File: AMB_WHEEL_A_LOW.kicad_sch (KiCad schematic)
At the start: 14 parts, among them U13 EPC2152, U14 EPC2152

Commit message: updated layouts, added motor
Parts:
- renumbered C103 to C127, C104 to C128, C105 to C129, C106 to C130, C107 to C131, C108 to C132, C109 to C133, C110 to C134, R75 to R131, R76 to R132, R77 to R133, R78 to R134, U13 to U11, U14 to U12

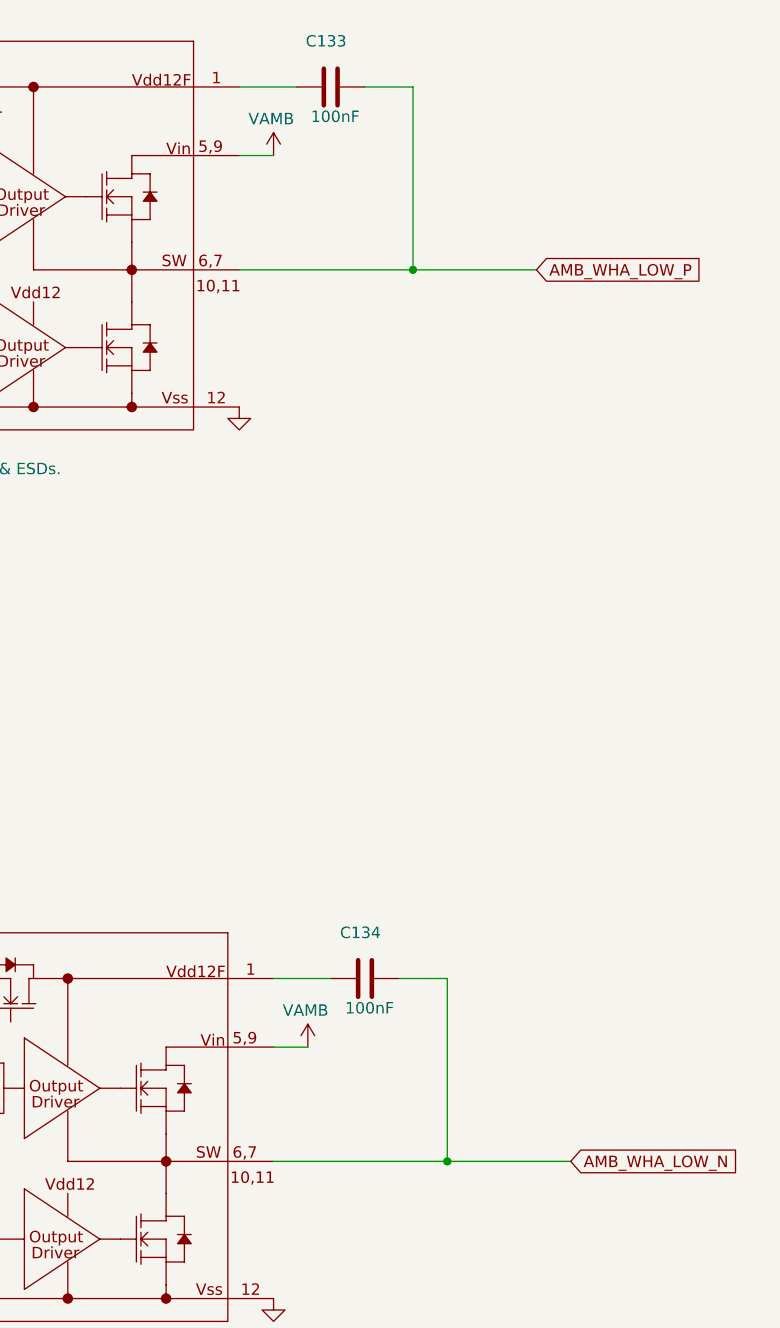
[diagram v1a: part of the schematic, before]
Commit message: Changes to layout pins
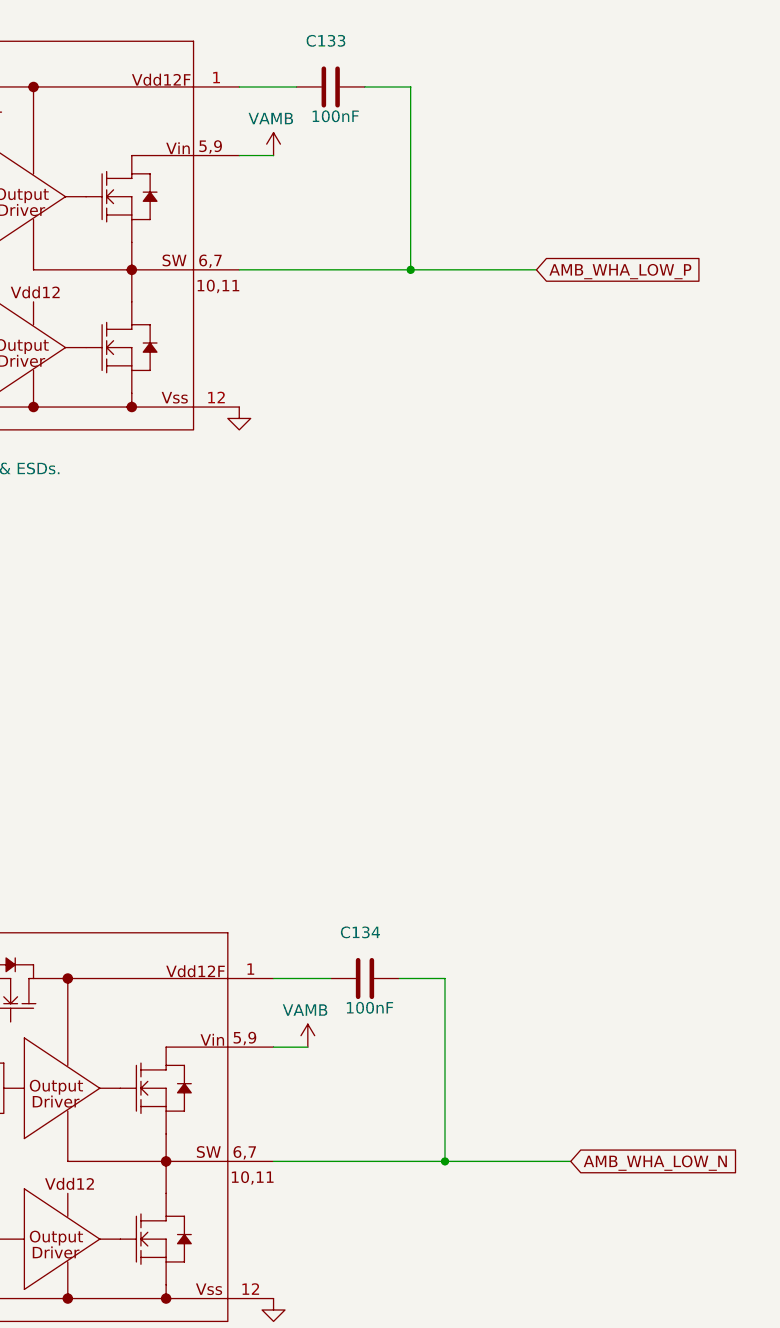
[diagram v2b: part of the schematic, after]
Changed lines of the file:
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@@
 	)
 	(junction
-		(at 189.484 58.42)
+		(at 189.23 58.42)
 		(diameter 0)
 		(color 0 0 0 0)
@@
 	)
 	(junction
-		(at 193.294 157.48)
+		(at 193.04 157.48)
 		(diameter 0)
 		(color 0 0 0 0)
@@
 	(wire
 		(pts
-			(xy 189.484 58.42) (xy 203.2 58.42)
+			(xy 189.23 58.42) (xy 203.2 58.42)
 		)
 		(stroke
@@
 	(wire
 		(pts
-			(xy 187.96 137.16) (xy 193.294 137.16)
+			(xy 187.96 137.16) (xy 193.04 137.16)
 		)
 		(stroke
@@
 	(wire
 		(pts
-			(xy 189.484 38.1) (xy 189.484 58.42)
+			(xy 189.23 38.1) (xy 189.23 58.42)
 		)
 		(stroke
@@
 	(wire
 		(pts
-			(xy 173.99 157.48) (xy 193.294 157.48)
+			(xy 173.99 157.48) (xy 193.04 157.48)
 		)
 		(stroke
@@
 	(wire
 		(pts
-			(xy 193.294 157.48) (xy 207.01 157.48)
+			(xy 193.04 157.48) (xy 207.01 157.48)
 		)
 		(stroke
@@
 	(wire
 		(pts
-			(xy 184.15 38.1) (xy 189.484 38.1)
+			(xy 184.15 38.1) (xy 189.23 38.1)
 		)
 		(stroke
@@
 	(wire
 		(pts
-			(xy 193.294 137.16) (xy 193.294 157.48)
+			(xy 193.04 137.16) (xy 193.04 157.48)
 		)
 		(stroke
@@
 	(wire
 		(pts
-			(xy 170.18 58.42) (xy 189.484 58.42)
+			(xy 170.18 58.42) (xy 189.23 58.42)
 		)
 		(stroke
@@
 	)
 	(symbol
-		(lib_id "CIAA_ACC:GND")
+		(lib_id "power:GND")
 		(at 170.18 73.66 0)
 		(unit 1)
@@
 		(property "Footprint" ""
 			(at 170.18 73.66 0)
+			(hide yes)
 			(show_name no)
 			(do_not_autoplace no)
@@
 		(property "Datasheet" ""
 			(at 170.18 73.66 0)
+			(hide yes)
 			(show_name no)
 			(do_not_autoplace no)
@@
 			)
 		)
-		(property "Description" ""
+		(property "Description" "Power symbol creates a global label with name \"GND\" , ground"
 			(at 170.18 73.66 0)
+			(hide yes)
 			(show_name no)
 			(do_not_autoplace no)
@@
 	)
 	(symbol
-		(lib_id "CIAA_ACC:GND")
+		(lib_id "power:GND")
 		(at 173.99 172.72 0)
 		(unit 1)
@@
 		(property "Footprint" ""
 			(at 173.99 172.72 0)
+			(hide yes)
 			(show_name no)
 			(do_not_autoplace no)
@@
 		(property "Datasheet" ""
 			(at 173.99 172.72 0)
+			(hide yes)
 			(show_name no)
 			(do_not_autoplace no)
@@
 			)
 		)
-		(property "Description" ""
+		(property "Description" "Power symbol creates a global label with name \"GND\" , ground"
 			(at 173.99 172.72 0)
+			(hide yes)
 			(show_name no)
 			(do_not_autoplace no)
@@
 	)
 	(symbol
-		(lib_id "CIAA_ACC:GND")
+		(lib_id "power:GND")
 		(at 109.22 73.66 0)
 		(unit 1)
@@
 		(property "Footprint" ""
 			(at 109.22 73.66 0)
+			(hide yes)
 			(show_name no)
 			(do_not_autoplace no)
@@
 		(property "Datasheet" ""
 			(at 109.22 73.66 0)
+			(hide yes)
 			(show_name no)
 			(do_not_autoplace no)
@@
 			)
 		)
-		(property "Description" ""
+		(property "Description" "Power symbol creates a global label with name \"GND\" , ground"
 			(at 109.22 73.66 0)
+			(hide yes)
 			(show_name no)
 			(do_not_autoplace no)
@@
 	)
 	(symbol
-		(lib_id "CIAA_ACC:GND")
+		(lib_id "power:GND")
 		(at 77.47 72.39 0)
 		(unit 1)
@@
 		(property "Footprint" ""
 			(at 77.47 72.39 0)
+			(hide yes)
 			(show_name no)
 			(do_not_autoplace no)
@@
 		(property "Datasheet" ""
 			(at 77.47 72.39 0)
+			(hide yes)
 			(show_name no)
 			(do_not_autoplace no)
@@
 			)
 		)
-		(property "Description" ""
+		(property "Description" "Power symbol creates a global label with name \"GND\" , ground"
 			(at 77.47 72.39 0)
+			(hide yes)
 			(show_name no)
 			(do_not_autoplace no)
@@
 	)
 	(symbol
-		(lib_id "CIAA_ACC:GND")
+		(lib_id "power:GND")
 		(at 104.14 46.99 0)
 		(unit 1)
@@
 		(property "Footprint" ""
 			(at 104.14 46.99 0)
+			(hide yes)
 			(show_name no)
 			(do_not_autoplace no)
@@
 		(property "Datasheet" ""
 			(at 104.14 46.99 0)
+			(hide yes)
 			(show_name no)
 			(do_not_autoplace no)
@@
 			)
 		)
-		(property "Description" ""
+		(property "Description" "Power symbol creates a global label with name \"GND\" , ground"
 			(at 104.14 46.99 0)
+			(hide yes)
 			(show_name no)
 			(do_not_autoplace no)
@@
 	)
 	(symbol
-		(lib_id "CIAA_ACC:GND")
+		(lib_id "power:GND")
 		(at 81.28 171.45 0)
 		(unit 1)
@@
 		(property "Footprint" ""
 			(at 81.28 171.45 0)
+			(hide yes)
 			(show_name no)
 			(do_not_autoplace no)
@@
 		(property "Datasheet" ""
 			(at 81.28 171.45 0)
+			(hide yes)
 			(show_name no)
 			(do_not_autoplace no)
@@
 			)
 		)
-		(property "Description" ""
+		(property "Description" "Power symbol creates a global label with name \"GND\" , ground"
 			(at 81.28 171.45 0)
+			(hide yes)
 			(show_name no)
 			(do_not_autoplace no)
@@
 	)
 	(symbol
-		(lib_id "CIAA_ACC:GND")
+		(lib_id "power:GND")
 		(at 85.09 156.21 0)
 		(unit 1)
@@
 		(property "Footprint" ""
 			(at 85.09 156.21 0)
+			(hide yes)
 			(show_name no)
 			(do_not_autoplace no)
@@
 		(property "Datasheet" ""
 			(at 85.09 156.21 0)
+			(hide yes)
 			(show_name no)
 			(do_not_autoplace no)
@@
 			)
 		)
-		(property "Description" ""
+		(property "Description" "Power symbol creates a global label with name \"GND\" , ground"
 			(at 85.09 156.21 0)
+			(hide yes)
 			(show_name no)
 			(do_not_autoplace no)
@@
 	)
 	(symbol
-		(lib_id "CIAA_ACC:GND")
+		(lib_id "power:GND")
 		(at 107.95 146.05 0)
 		(unit 1)
@@
 		(property "Footprint" ""
 			(at 107.95 146.05 0)
+			(hide yes)
 			(show_name no)
 			(do_not_autoplace no)
@@
 		(property "Datasheet" ""
 			(at 107.95 146.05 0)
+			(hide yes)
 			(show_name no)
 			(do_not_autoplace no)
@@
 			)
 		)
-		(property "Description" ""
+		(property "Description" "Power symbol creates a global label with name \"GND\" , ground"
 			(at 107.95 146.05 0)
+			(hide yes)
 			(show_name no)
 			(do_not_autoplace no)
@@
 	)
 	(symbol
-		(lib_id "CIAA_ACC:GND")
+		(lib_id "power:GND")
 		(at 52.07 105.41 0)
 		(unit 1)
@@
 		(property "Footprint" ""
 			(at 52.07 105.41 0)
+			(hide yes)
 			(show_name no)
 			(do_not_autoplace no)
@@
 		(property "Datasheet" ""
 			(at 52.07 105.41 0)
+			(hide yes)
 			(show_name no)
 			(do_not_autoplace no)
@@
 			)
 		)
-		(property "Description" ""
+		(property "Description" "Power symbol creates a global label with name \"GND\" , ground"
 			(at 52.07 105.41 0)
+			(hide yes)
 			(show_name no)
 			(do_not_autoplace no)
@@
 	)
 	(symbol
-		(lib_id "CIAA_ACC:GND")
+		(lib_id "power:GND")
 		(at 81.28 57.15 0)
 		(unit 1)
@@
 		(property "Footprint" ""
 			(at 81.28 57.15 0)
+			(hide yes)
 			(show_name no)
 			(do_not_autoplace no)
@@
 		(property "Datasheet" ""
 			(at 81.28 57.15 0)
+			(hide yes)
 			(show_name no)
 			(do_not_autoplace no)
@@
 			)
 		)
-		(property "Description" ""
+		(property "Description" "Power symbol creates a global label with name \"GND\" , ground"
 			(at 81.28 57.15 0)
+			(hide yes)
 			(show_name no)
 			(do_not_autoplace no)
@@
 	)
 	(symbol
-		(lib_id "CIAA_ACC:GND")
+		(lib_id "power:GND")
 		(at 113.03 172.72 0)
 		(unit 1)
@@
 		(property "Footprint" ""
 			(at 113.03 172.72 0)
+			(hide yes)
 			(show_name no)
 			(do_not_autoplace no)
@@
 		(property "Datasheet" ""
 			(at 113.03 172.72 0)
+			(hide yes)
 			(show_name no)
 			(do_not_autoplace no)
@@
 			)
 		)
-		(property "Description" ""
+		(property "Description" "Power symbol creates a global label with name \"GND\" , ground"
 			(at 113.03 172.72 0)
+			(hide yes)
 			(show_name no)
 			(do_not_autoplace no)
